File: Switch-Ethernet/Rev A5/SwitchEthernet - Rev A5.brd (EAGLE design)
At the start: 86 x 90 mm, 122 parts, among them J1 22-05-7028-02, J2 NE8FAV, J3 NE8FAV, J4 DF17(4.0)-20DS-0.5V(57), J5 DF17(4.0)-20DP-0.5V(57), J6 RB1-125BAG1A, T1 H1102FNL, T2 H1102FNL, T3 EXMACHINA-LOGO-NAME, U1 TC1264-3.3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

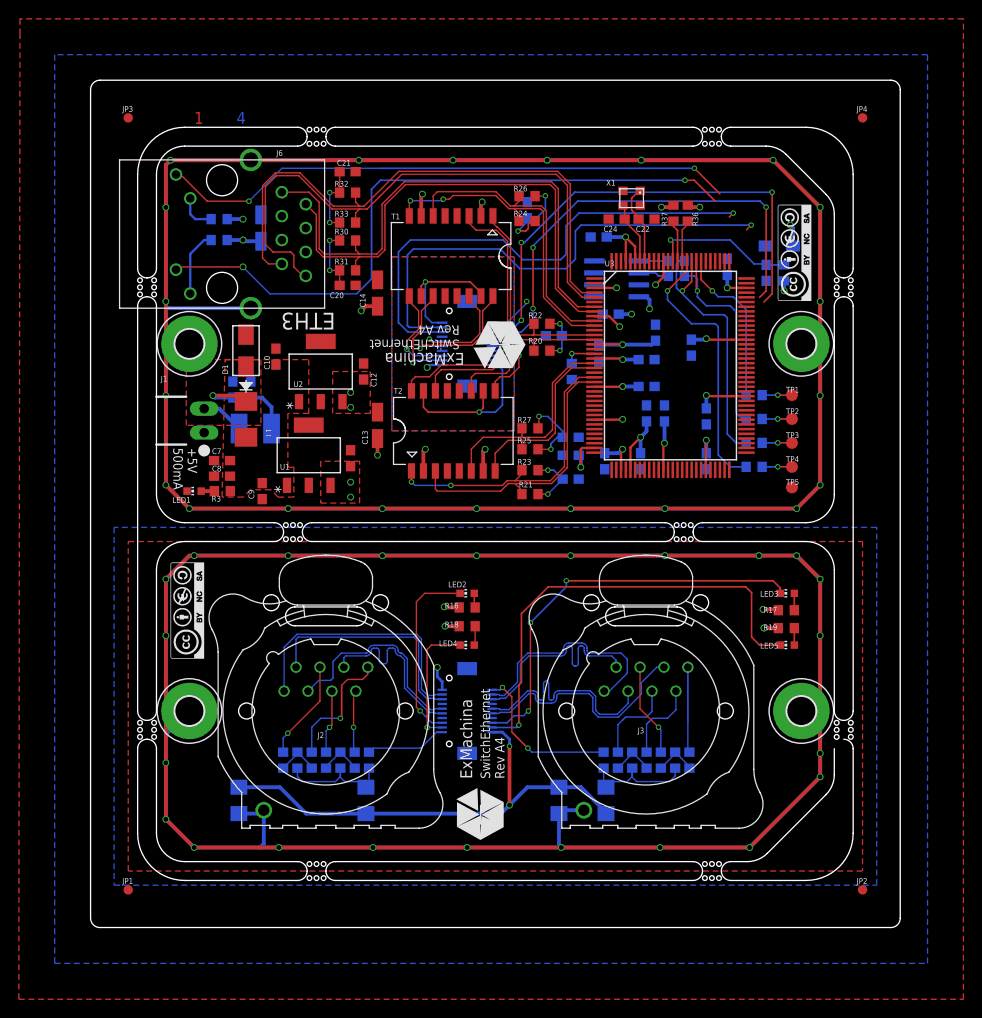
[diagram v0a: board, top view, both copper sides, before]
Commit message: Re-route the ethernet leds
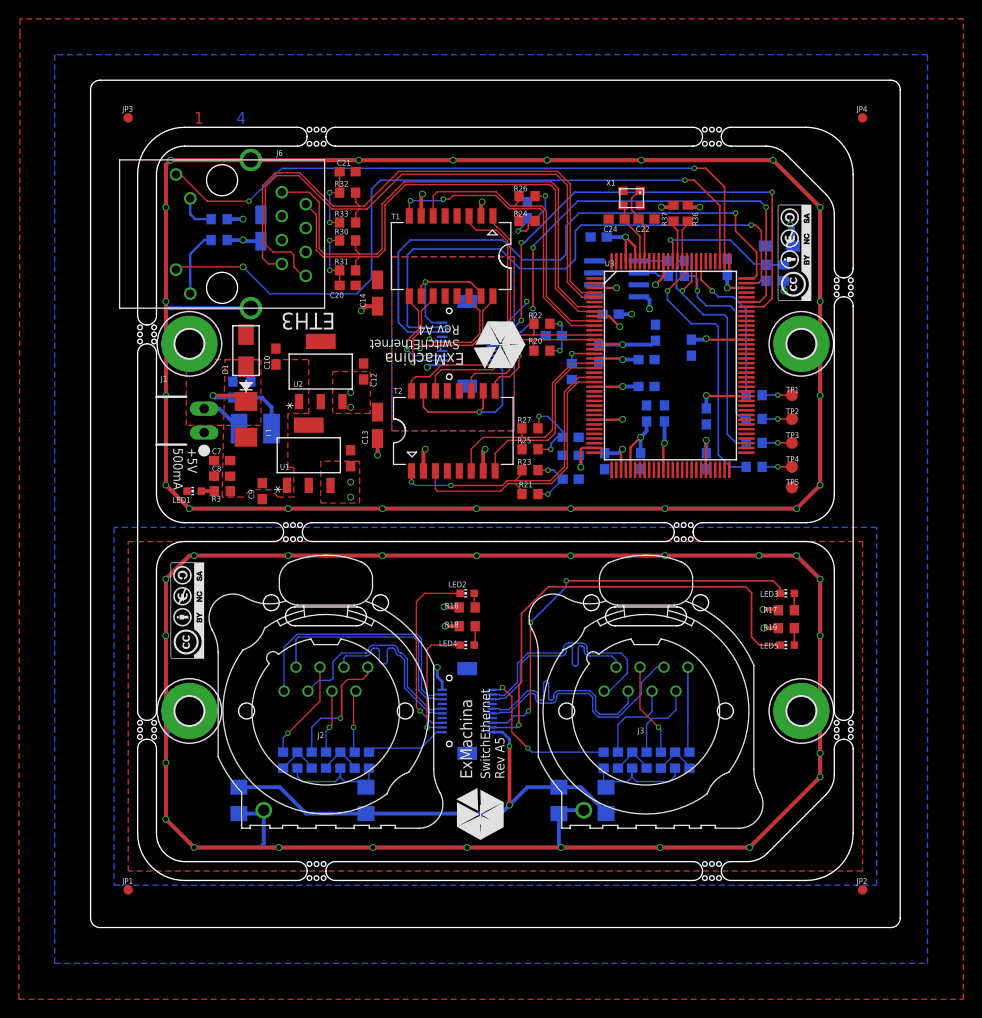
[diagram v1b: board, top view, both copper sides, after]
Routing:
- net L1-1: track 73.6 -> 82.0 mm
- net L3-2: track 61.5 -> 69.6 mm
- net L1-2: track 66.9 -> 74.5 mm
- net L3-1: track 70.1 -> 76.7 mm
- net L2-2: track 101.4 -> 103.8 mm
- net L2-1: track 93.4 -> 95.3 mm
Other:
- outline, holes or cut-outs redrawn
- board text added: "SwitchEthernet Rev A5"
